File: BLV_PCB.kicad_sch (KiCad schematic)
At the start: 13 parts, among them J1 JST-PH, J2 JST-PH, J3 JST-PH, J4 PinHeader_01x03_Pin, J5 PinHeader_01x03_Pin, J6 PinHeader_01x03_Pin, J7 Conn_02x03_Odd_Even

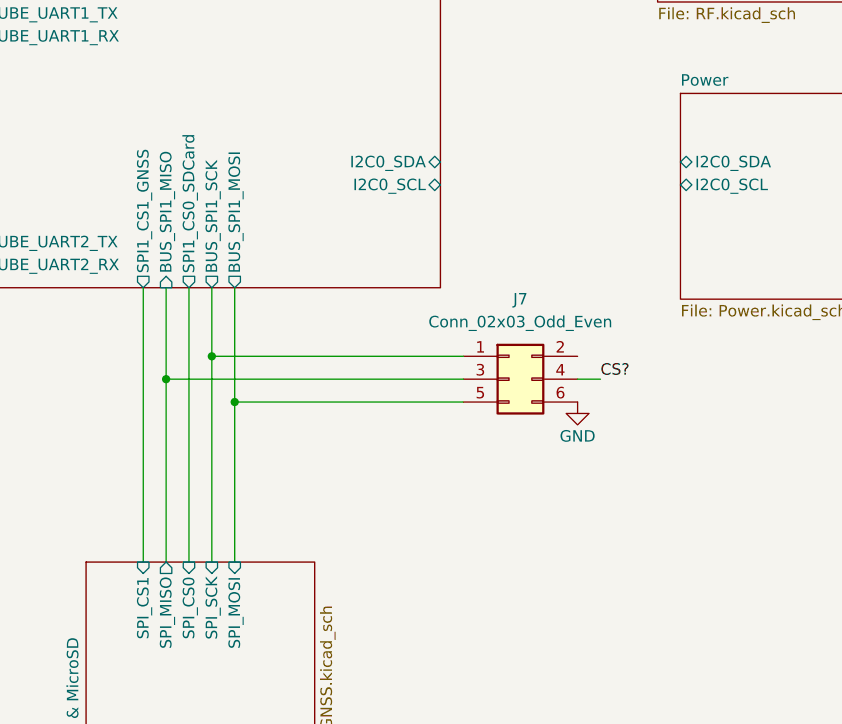
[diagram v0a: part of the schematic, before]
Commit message: Finish preliminary power layout
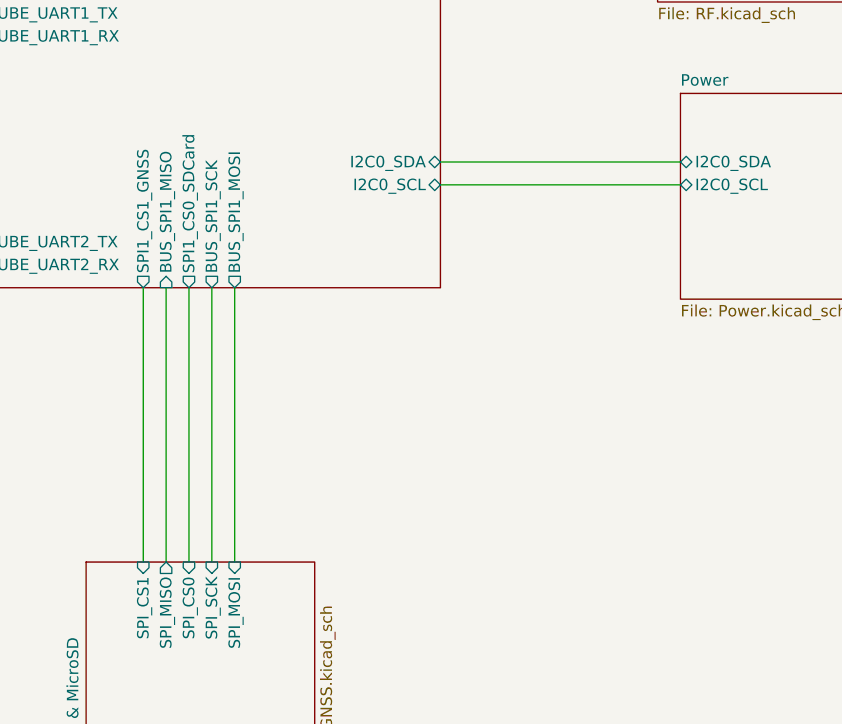
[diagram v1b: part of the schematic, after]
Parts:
- removed J7: Conn_02x03_Odd_Even, Connector_PinHeader_2.54mm:PinHeader_2x03_P2.54mm_Vertical, symbol Connector_Generic:Conn_02x03_Odd_Even
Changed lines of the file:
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@@
-	)
-	(junction
-		(at 166.37 142.24)
-		(diameter 0)
-		(color 0 0 0 0)
 	)
 	(junction
@@
 	)
 	(junction
-		(at 161.29 144.78)
-		(diameter 0)
-		(color 0 0 0 0)
-	)
-	(junction
-		(at 168.91 147.32)
-		(diameter 0)
-		(color 0 0 0 0)
-	)
-	(junction
 		(at 101.6 129.54)
 		(diameter 0)
@@
 	(wire
 		(pts
-			(xy 168.91 134.62) (xy 168.91 147.32)
-		)
-		(stroke
-			(width 0)
-			(type default)
-		)
-	)
-	(wire
-		(pts
 			(xy 191.77 91.44) (xy 215.9 91.44)
 		)
@@
 	(wire
 		(pts
-			(xy 161.29 144.78) (xy 194.31 144.78)
-		)
-		(stroke
-			(width 0)
-			(type default)
-		)
-	)
-	(wire
-		(pts
 			(xy 81.28 111.76) (xy 82.55 111.76)
 		)
@@
 	(wire
 		(pts
+			(xy 191.77 123.19) (xy 218.44 123.19)
+		)
+		(stroke
+			(width 0)
+			(type default)
+		)
+	)
+	(wire
+		(pts
 			(xy 191.77 83.82) (xy 215.9 83.82)
 		)
@@
 	(wire
 		(pts
+			(xy 191.77 120.65) (xy 218.44 120.65)
+		)
+		(stroke
+			(width 0)
+			(type default)
+		)
+	)
+	(wire
+		(pts
 			(xy 101.6 143.51) (xy 99.06 143.51)
 		)
@@
 	(wire
 		(pts
-			(xy 168.91 147.32) (xy 168.91 165.1)
-		)
-		(stroke
-			(width 0)
-			(type default)
-		)
-	)
-	(wire
-		(pts
-			(xy 161.29 144.78) (xy 161.29 165.1)
+			(xy 168.91 134.62) (xy 168.91 165.1)
 		)
 		(stroke
@@
 	(wire
 		(pts
-			(xy 168.91 147.32) (xy 194.31 147.32)
-		)
-		(stroke
-			(width 0)
-			(type default)
-		)
-	)
-	(wire
-		(pts
 			(xy 158.75 134.62) (xy 158.75 165.1)
 		)
@@
 	(wire
 		(pts
-			(xy 166.37 134.62) (xy 166.37 142.24)
+			(xy 166.37 134.62) (xy 166.37 165.1)
 		)
 		(stroke
@@
 	(wire
 		(pts
-			(xy 161.29 134.62) (xy 161.29 144.78)
+			(xy 161.29 134.62) (xy 161.29 165.1)
 		)
 		(stroke
@@
 	(wire
 		(pts
-			(xy 209.55 144.78) (xy 207.01 144.78)
-		)
-		(stroke
-			(width 0)
-			(type default)
-		)
-	)
-	(wire
-		(pts
 			(xy 81.28 132.08) (xy 97.79 132.08)
 		)
@@
 	(wire
 		(pts
-			(xy 166.37 142.24) (xy 166.37 165.1)
-		)
-		(stroke
-			(width 0)
-			(type default)
-		)
-	)
-	(wire
-		(pts
 			(xy 101.6 129.54) (xy 119.38 129.54)
 		)
@@
 		(pts
 			(xy 101.6 129.54) (xy 101.6 134.62)
-		)
-		(stroke
-			(width 0)
-			(type default)
-		)
-	)
-	(wire
-		(pts
-			(xy 166.37 142.24) (xy 194.31 142.24)
 		)
 		(stroke
@@
 	(label "Cube0_UART_TX"
 		(at 123.19 78.74 0)
-		(effects
-			(font
-				(size 1.27 1.27)
-			)
-			(justify left bottom)
-		)
-	)
-	(label "CS?"
-		(at 209.55 144.78 0)
 		(effects
 			(font
@@
 	)
 	(symbol
-		(lib_id "Connector_Generic:Conn_02x03_Odd_Even")
-		(at 199.39 144.78 0)
-		(unit 1)
-		(exclude_from_sim no)
-		(in_bom yes)
-		(on_board yes)
-		(dnp no)
-		(fields_autoplaced yes)
-		(property "Reference" "J7"
-			(at 200.66 135.89 0)
-			(effects
-				(font
-					(size 1.27 1.27)
-				)
-			)
-		)
-		(property "Value" "Conn_02x03_Odd_Even"
-			(at 200.66 138.43 0)
-			(effects
-				(font
-					(size 1.27 1.27)
-				)
-			)
-		)
-		(property "Footprint" "Connector_PinHeader_2.54mm:PinHeader_2x03_P2.54mm_Vertical"
-			(at 199.39 144.78 0)
-			(effects
-				(font
-					(size 1.27 1.27)
-				)
-				(hide yes)
-			)
-		)
-		(property "Datasheet" "~"
-			(at 199.39 144.78 0)
-			(effects
-				(font
-					(size 1.27 1.27)
-				)
-				(hide yes)
-			)
-		)
-		(property "Description" "Generic connector, double row, 02x03, odd/even pin numbering scheme (row 1 odd numbers, row 2 even numbers), script generated (kicad-library-utils/schlib/autogen/connector/)"
-			(at 199.39 144.78 0)
-			(effects
-				(font
-					(size 1.27 1.27)
-				)
-				(hide yes)
-			)
-		)
-		(pin "5"
-		)
-		(pin "2"
-		)
-		(pin "1"
-		)
-		(pin "6"
-		)
-		(pin "3"
-		)
-		(pin "4"
-		)
-		(instances
-			(project ""
-				(path "/e98ed281-6a46-49b2-ab41-e3d95fdf6973"
-					(reference "J7")
-					(unit 1)
-				)
-			)
-		)
-	)
-	(symbol
 		(lib_id "power:GND")
 		(at 82.55 137.16 0)
@@
 					(unit 1)
 				)
-			)
-		)
-	)
-	(symbol
-		(lib_id "power:GND")
-		(at 207.01 147.32 0)
-		(unit 1)
-		(exclude_from_sim no)
-		(in_bom yes)
-		(on_board yes)
-		(dnp no)
-		(property "Reference" "#PWR08"
-			(at 207.01 153.67 0)
-			(effects
-				(font
-					(size 1.27 1.27)
-				)
-				(hide yes)
-			)
-		)
-		(property "Value" "GND"
-			(at 207.01 151.13 0)
-			(effects
-				(font
-					(size 1.27 1.27)
-				)
-			)
-		)
-		(property "Footprint" ""
-			(at 207.01 147.32 0)
-			(effects
-				(font
-					(size 1.27 1.27)
-				)
-				(hide yes)
-			)
-		)
-		(property "Datasheet" ""
-			(at 207.01 147.32 0)
-			(effects
-				(font
-					(size 1.27 1.27)
-				)
-				(hide yes)
-			)
-		)
-		(property "Description" "Power symbol creates a global label with name \"GND\" , ground"
-			(at 207.01 147.32 0)
-			(effects
-				(font
-					(size 1.27 1.27)
-				)
-				(hide yes)
-			)
-		)
-		(pin "1"
-		)
-		(instances
-			(project "BLV_PCB"
-				(path "/e98ed281-6a46-49b2-ab41-e3d95fdf6973"
-					(reference "#PWR08")
-					(unit 1)
-				)

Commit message: v2 layouts done
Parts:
- renumbered D1 to D31, D2 to D32, H1 to H31, H2 to H32, H3 to H33, H4 to H34, J1 to J31, J2 to J32, J3 to J33, J6 to J34, J4 to J35, J5 to J36
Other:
- added sheet sensors (sensors.kicad_sch)
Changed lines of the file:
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@@
+	)
+	(junction
+		(at 212.09 120.65)
+		(diameter 0)
+		(color 0 0 0 0)
 	)
 	(junction
@@
 	)
 	(junction
+		(at 209.55 123.19)
+		(diameter 0)
+		(color 0 0 0 0)
+	)
+	(junction
 		(at 119.38 104.14)
 		(diameter 0)
@@
 	(wire
 		(pts
+			(xy 218.44 161.29) (xy 209.55 161.29)
+		)
+		(stroke
+			(width 0)
+			(type default)
+		)
+	)
+	(wire
+		(pts
 			(xy 191.77 81.28) (xy 215.9 81.28)
 		)
@@
 	(wire
 		(pts
-			(xy 191.77 123.19) (xy 218.44 123.19)
+			(xy 191.77 123.19) (xy 209.55 123.19)
 		)
 		(stroke
@@
 	(wire
 		(pts
-			(xy 191.77 120.65) (xy 218.44 120.65)
+			(xy 191.77 120.65) (xy 212.09 120.65)
 		)
 		(stroke
@@
 	(wire
 		(pts
+			(xy 209.55 161.29) (xy 209.55 123.19)
+		)
+		(stroke
+			(width 0)
+			(type default)
+		)
+	)
+	(wire
+		(pts
 			(xy 93.98 91.44) (xy 119.38 91.44)
 		)
@@
 	(wire
 		(pts
+			(xy 212.09 120.65) (xy 218.44 120.65)
+		)
+		(stroke
+			(width 0)
+			(type default)
+		)
+	)
+	(wire
+		(pts
 			(xy 101.6 142.24) (xy 101.6 143.51)
 		)
@@
 	(wire
 		(pts
+			(xy 212.09 158.75) (xy 212.09 120.65)
+		)
+		(stroke
+			(width 0)
+			(type default)
+		)
+	)
+	(wire
+		(pts
 			(xy 166.37 134.62) (xy 166.37 165.1)
 		)
@@
 	(wire
 		(pts
+			(xy 218.44 158.75) (xy 212.09 158.75)
+		)
+		(stroke
+			(width 0)
+			(type default)
+		)
+	)
+	(wire
+		(pts
 			(xy 81.28 132.08) (xy 97.79 132.08)
 		)
@@
 		(pts
 			(xy 119.38 129.54) (xy 119.38 154.94)
+		)
+		(stroke
+			(width 0)
+			(type default)
+		)
+	)
+	(wire
+		(pts
+			(xy 209.55 123.19) (xy 218.44 123.19)
 		)
 		(stroke
@@
 		(on_board yes)
 		(dnp no)
-		(property "Reference" "J2"
+		(property "Reference" "J32"
 			(at 74.168 105.918 0)
 			(effects
@@
 			(project "BLV_PCB"
 				(path "/e98ed281-6a46-49b2-ab41-e3d95fdf6973"
-					(reference "J2")
+					(reference "J32")
 					(unit 1)
 				)
@@
 		(on_board yes)
 		(dnp no)
-		(property "Reference" "#PWR04"
+		(property "Reference" "#PWR035"
 			(at 95.25 102.87 0)
 			(effects
@@
 			(project "BLV_PCB"
 				(path "/e98ed281-6a46-49b2-ab41-e3d95fdf6973"
-					(reference "#PWR04")
+					(reference "#PWR035")
 					(unit 1)
 				)
@@
 		(on_board yes)
 		(dnp no)
-		(property "Reference" "#PWR05"
+		(property "Reference" "#PWR036"
 			(at 95.25 128.27 0)
 			(effects
@@
 			(project "BLV_PCB"
 				(path "/e98ed281-6a46-49b2-ab41-e3d95fdf6973"
-					(reference "#PWR05")
+					(reference "#PWR036")
 					(unit 1)
 				)
@@
 		(on_board yes)
 		(dnp no)
-		(property "Reference" "#PWR03"
+		(property "Reference" "#PWR033"
 			(at 82.55 143.51 0)
 			(effects
@@
 			(project "BLV_PCB"
 				(path "/e98ed281-6a46-49b2-ab41-e3d95fdf6973"
-					(reference "#PWR03")
+					(reference "#PWR033")
 					(unit 1)
 				)
@@
 		(on_board yes)
 		(dnp no)
-		(property "Reference" "#PWR01"
+		(property "Reference" "#PWR031"
 			(at 82.55 92.71 0)
 			(effects
@@
 			(project "BLV_PCB"
 				(path "/e98ed281-6a46-49b2-ab41-e3d95fdf6973"
-					(reference "#PWR01")
+					(reference "#PWR031")
 					(unit 1)
 				)
@@
 		(on_board yes)
 		(dnp no)
-		(property "Reference" "#PWR02"
+		(property "Reference" "#PWR032"
 			(at 82.55 118.11 0)
 			(effects
@@
 			(project "BLV_PCB"
 				(path "/e98ed281-6a46-49b2-ab41-e3d95fdf6973"
-					(reference "#PWR02")
+					(reference "#PWR032")
 					(unit 1)
 				)
@@
 		(on_board yes)
 		(dnp no)
-		(property "Reference" "J6"
+		(property "Reference" "J34"
 			(at 85.598 159.512 0)
 			(effects
@@
 			(project "BLV_PCB"
 				(path "/e98ed281-6a46-49b2-ab41-e3d95fdf6973"
-					(reference "J6")
+					(reference "J34")
 					(unit 1)
 				)
@@
 		(on_board yes)
 		(dnp no)
-		(property "Reference" "J3"
+		(property "Reference" "J33"
 			(at 74.168 131.318 0)
 			(effects
@@
 			(project "BLV_PCB"
 				(path "/e98ed281-6a46-49b2-ab41-e3d95fdf6973"
-					(reference "J3")
+					(reference "J33")
 					(unit 1)
 				)
@@
 		(on_board yes)
 		(dnp no)
-		(property "Reference" "H2"
+		(property "Reference" "H32"
 			(at 294.64 250.1899 0)
 			(effects
@@
 			(project "BLV_PCB"
 				(path "/e98ed281-6a46-49b2-ab41-e3d95fdf6973"
-					(reference "H2")
+					(reference "H32")
 					(unit 1)
 				)
@@
 		(on_board yes)
 		(dnp no)
-		(property "Reference" "J1"
+		(property "Reference" "J31"
 			(at 74.168 80.518 0)
 			(effects
@@
 			(project "BLV_PCB"
 				(path "/e98ed281-6a46-49b2-ab41-e3d95fdf6973"
-					(reference "J1")
+					(reference "J31")
 					(unit 1)
 				)
@@
 		(on_board yes)
 		(dnp no)
-		(property "Reference" "H3"
+		(property "Reference" "H33"
 			(at 294.64 255.2699 0)
 			(effects
@@
 			(project "BLV_PCB"
 				(path "/e98ed281-6a46-49b2-ab41-e3d95fdf6973"
-					(reference "H3")
+					(reference "H33")
 					(unit 1)
 				)
@@
 		(on_board yes)
 		(dnp no)
-		(property "Reference" "H4"
+		(property "Reference" "H34"
 			(at 294.64 260.3499 0)
 			(effects
@@
 			(project "BLV_PCB"
 				(path "/e98ed281-6a46-49b2-ab41-e3d95fdf6973"
-					(reference "H4")
+					(reference "H34")
 					(unit 1)
 				)
@@
 		(on_board yes)
 		(dnp no)
-		(property "Reference" "J4"
+		(property "Reference" "J35"
 			(at 86.868 96.012 0)
 			(effects
@@
 			(project ""
 				(path "/e98ed281-6a46-49b2-ab41-e3d95fdf6973"
-					(reference "J4")
+					(reference "J35")
 					(unit 1)
 				)
@@
 		(dnp no)
 		(fields_autoplaced yes)
-		(property "Reference" "D2"
+		(property "Reference" "D32"
 			(at 104.14 137.1599 90)
 			(effects
@@
 			(project "BLV_PCB"
 				(path "/e98ed281-6a46-49b2-ab41-e3d95fdf6973"
-					(reference "D2")
+					(reference "D32")
 					(unit 1)
 				)
@@
 		(on_board yes)
 		(dnp no)
-		(property "Reference" "D1"
+		(property "Reference" "D31"
 			(at 95.25 137.1599 90)
 			(effects
@@
 			(project "BLV_PCB"
 				(path "/e98ed281-6a46-49b2-ab41-e3d95fdf6973"
-					(reference "D1")
+					(reference "D31")
 					(unit 1)
 				)
@@
 		(on_board yes)
 		(dnp no)
-		(property "Reference" "#PWR041"
+		(property "Reference" "#PWR037"
 			(at 99.06 149.86 0)
 			(effects
@@
 			(project "BLV_PCB"
 				(path "/e98ed281-6a46-49b2-ab41-e3d95fdf6973"
-					(reference "#PWR041")
+					(reference "#PWR037")
 					(unit 1)
 				)
@@
 		(on_board yes)
 		(dnp no)
-		(property "Reference" "H1"
+		(property "Reference" "H31"
 			(at 294.64 245.1099 0)
 			(effects
@@
 			(project "BLV_PCB"
 				(path "/e98ed281-6a46-49b2-ab41-e3d95fdf6973"
-					(reference "H1")
+					(reference "H31")
 					(unit 1)
 				)
@@
 		(on_board yes)
 		(dnp no)
-		(property "Reference" "J5"
+		(property "Reference" "J36"
 			(at 86.868 121.412 0)
 			(effects
@@
 			(project "BLV_PCB"
 				(path "/e98ed281-6a46-49b2-ab41-e3d95fdf6973"
-					(reference "J5")
+					(reference "J36")
 					(unit 1)
 				)
@@
 		(on_board yes)
 		(dnp no)
-		(property "Reference" "#PWR06"
+		(property "Reference" "#PWR034"
 			(at 93.98 166.37 0)
 			(effects
@@
 			(project "BLV_PCB"
 				(path "/e98ed281-6a46-49b2-ab41-e3d95fdf6973"
-					(reference "#PWR06")
+					(reference "#PWR034")
 					(unit 1)
 				)
 			)
+		)
+	)
+	(sheet
+		(at 218.44 149.86)
+		(size 33.02 19.05)
+		(exclude_from_sim no)
+		(in_bom yes)
+		(on_board yes)
+		(dnp no)
+		(fields_autoplaced yes)
+		(stroke
+			(width 0.1524)
+			(type solid)
+		)
+		(fill
+			(color 0 0 0 0.0000)
+		)
+		(property "Sheetname" "sensors"
+			(at 218.44 149.1484 0)
+			(effects
+				(font
+					(size 1.27 1.27)
+				)
+				(justify left bottom)
+			)
+		)
+		(property "Sheetfile" "sensors.kicad_sch"
+			(at 218.44 169.4946 0)
+			(effects
+				(font
+					(size 1.27 1.27)
+				)
+				(justify left top)
+			)
+		)
+		(pin "I2C0_SCL" bidirectional
+			(at 218.44 161.29 180)
+			(effects
+				(font
+					(size 1.27 1.27)
+				)
+				(justify left)
+			)
+		)
+		(pin "I2C0_SDA" bidirectional
+			(at 218.44 158.75 180)
+			(effects
+				(font
+					(size 1.27 1.27)
+				)
+				(justify left)
+			)
+		)
+		(instances
+			(project "BLV_PCB"
+				(path "/e98ed281-6a46-49b2-ab41-e3d95fdf6973"
+					(page "7")
+				)
+			)

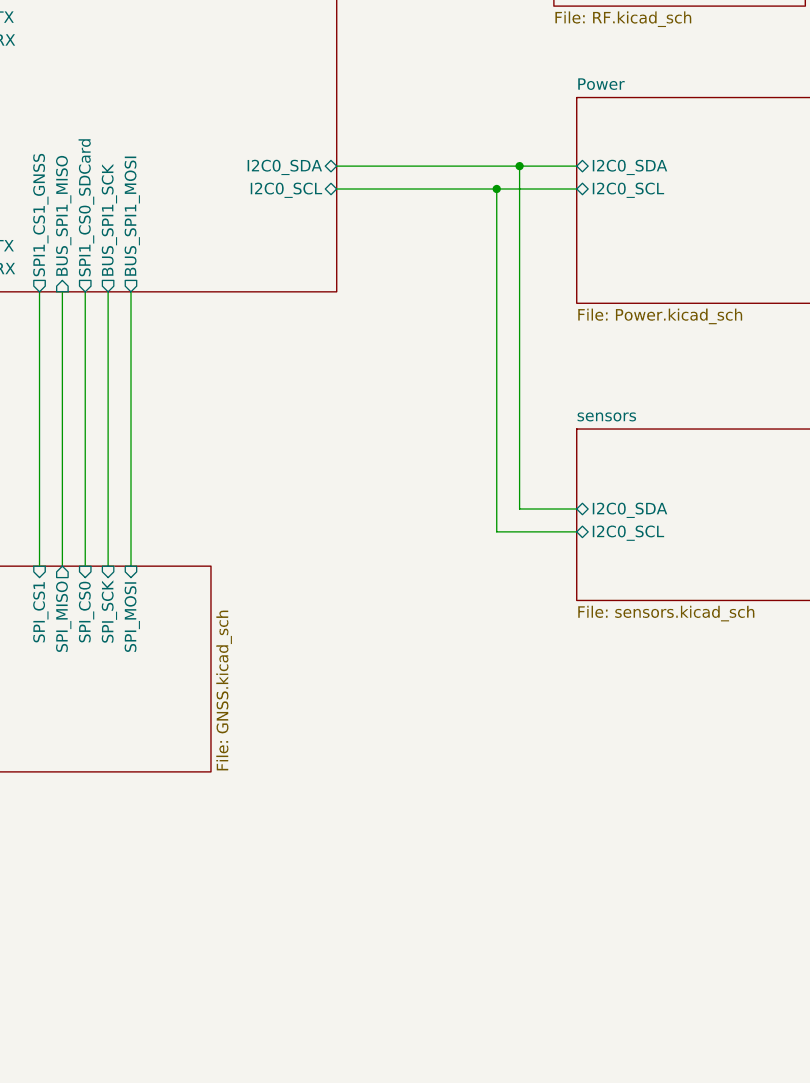
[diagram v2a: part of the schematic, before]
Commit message: Final production changes
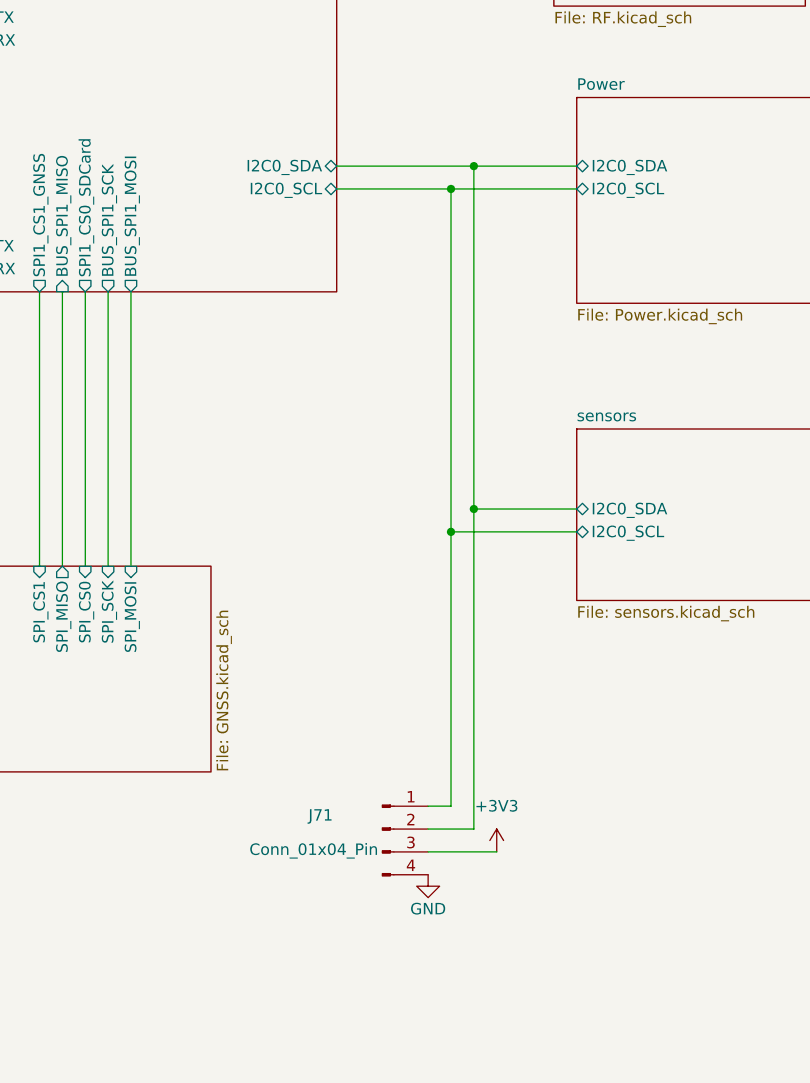
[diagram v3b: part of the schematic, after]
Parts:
- added J71: Conn_01x04_Pin, Connector_PinHeader_2.54mm:PinHeader_1x04_P2.54mm_Vertical, symbol Connector:Conn_01x04_Pin
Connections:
- net GND: now also J71.4 (Pin_4)
- net MCU/I2C0_SCL: now also J71.1 (Pin_1)
- net MCU/I2C0_SDA: now also J71.2 (Pin_2)
- new net +3V3: J71.3 (Pin_3)
